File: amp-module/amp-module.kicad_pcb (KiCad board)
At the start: 2 copper layers, 80 x 22 mm, 28 parts, among them IC1 AD5245BRJZ10-RL7, U5 TPA3221DDVR

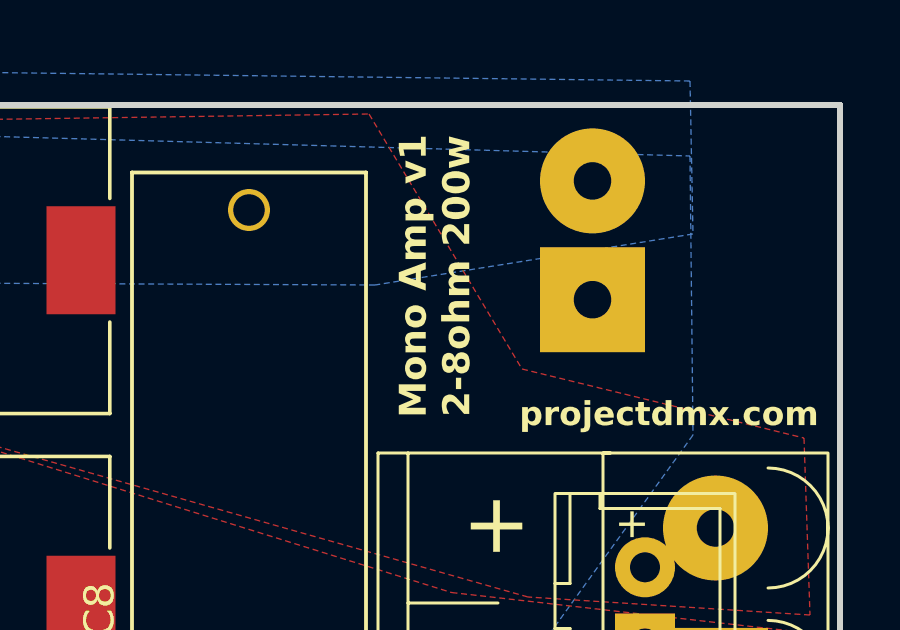
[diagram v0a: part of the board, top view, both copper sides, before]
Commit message: move mounting holes on modules and controller
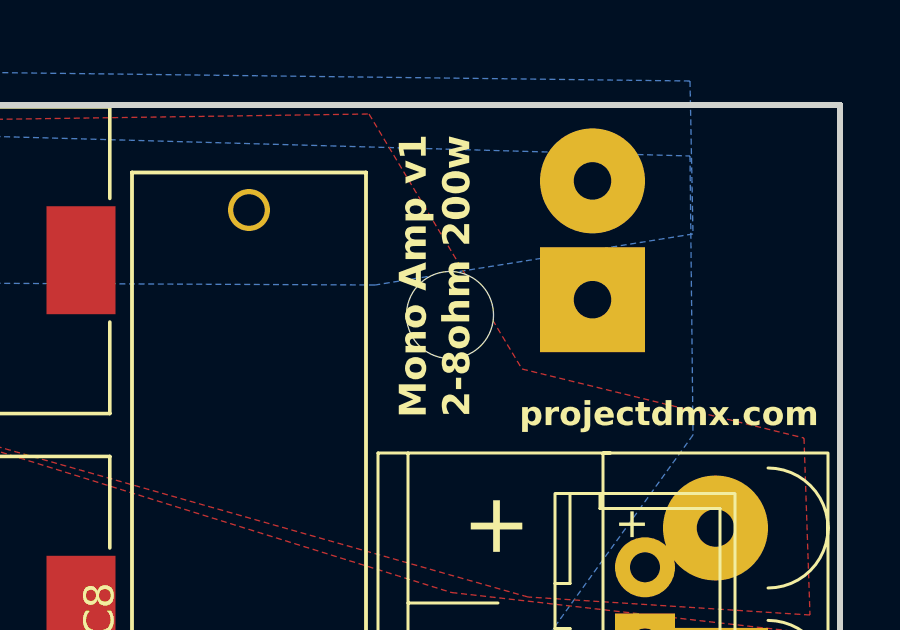
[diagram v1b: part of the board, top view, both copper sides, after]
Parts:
- added ?: , , F.Cu at (197.2, 76.0)
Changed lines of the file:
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@@
 		)
+	)
+	(footprint ""
+		(layer "F.Cu")
+		(at 197.2 76)
+		(property "Reference" ""
+			(at 0 0 0)
+			(layer "F.SilkS")
+			(effects
+				(font
+					(size 1.27 1.27)
+					(thickness 0.15)
+				)
+			)
+		)
+		(property "Value" ""
+			(at 0 0 0)
+			(layer "F.Fab")
+			(effects
+				(font
+					(size 1.27 1.27)
+					(thickness 0.15)
+				)
+			)
+		)
+		(property "Datasheet" ""
+			(at 0 0 0)
+			(layer "F.Fab")
+			(hide yes)
+			(effects
+				(font
+					(size 1.27 1.27)
+					(thickness 0.15)
+				)
+			)
+		)
+		(property "Description" ""
+			(at 0 0 0)
+			(layer "F.Fab")
+			(hide yes)
+			(effects
+				(font
+					(size 1.27 1.27)
+					(thickness 0.15)
+				)
+			)
+		)
+		(pad "" np_thru_hole circle
+			(at -13 7)
+			(size 2.9 2.9)
+			(drill 2.9)
+			(layers "*.Cu" "*.Mask")
+		)
+		(embedded_fonts no)
 	)
 	(footprint "ProjectDMX:Module Interface"

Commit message: cleanup footprints and layout
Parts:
- C10, C6: footprint PCM_JLCPCB:C_0402 -> Capacitor_SMD:C_0603_1608Metric_Pad1.08x0.95mm_HandSolder
- C11, C12, C13, C14, C3, C4, C5, C7: footprint PCM_JLCPCB:C_0603 -> Capacitor_SMD:C_0603_1608Metric_Pad1.08x0.95mm_HandSolder
- C9: footprint Imported:GMK316BJ105KLHT -> Capacitor_SMD:C_0603_1608Metric_Pad1.08x0.95mm_HandSolder
- R1, R2, R3, R4, R6, R7: footprint PCM_JLCPCB:R_0603 -> Resistor_SMD:R_0603_1608Metric_Pad0.98x0.95mm_HandSolder
- moved C6 1.91 mm to (146.5, 77.9)
- moved R2 1.73 mm to (146.5, 86.0)
- moved C5 1.59 mm to (146.3, 84.1)
- moved C10 1.36 mm to (146.2, 79.5)
- moved C4 1.33 mm to (146.3, 82.5)
- moved R7 1.28 mm to (144.3, 96.0)
- moved C7 0.30 mm to (159.2, 93.0)
- moved C14 0.22 mm to (146.5, 92.8)
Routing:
- net 5V: track 56.6 -> 60.1 mm
- net Net-(U1-AGP4): track 52.0 -> 49.2 mm
- net Net-(U1-GP3): track 39.1 -> 41.5 mm
- net Net-(IC1-W): track 19.6 -> 18.8 mm
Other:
- board text added: "5-24v"
- board text added: "A: 1110"
